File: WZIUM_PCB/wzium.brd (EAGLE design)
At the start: 100 x 100 mm, 21 parts, among them IC1 ATMEGA328PB-AU, J2 RASPBERRYPI-40-PIN-GPIO_PTH_M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

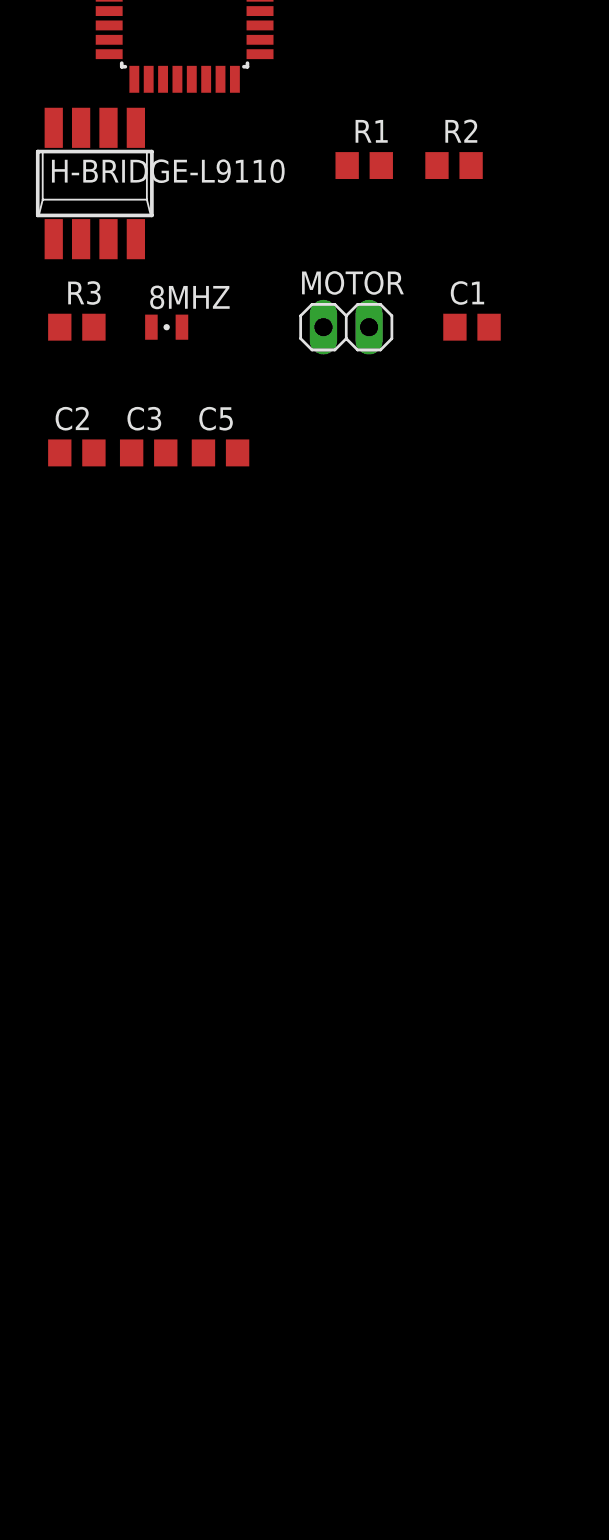
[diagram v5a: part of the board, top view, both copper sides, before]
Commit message: dodano sekcje czujnikow odleglosci Sharp GP2Y0A41SK0F
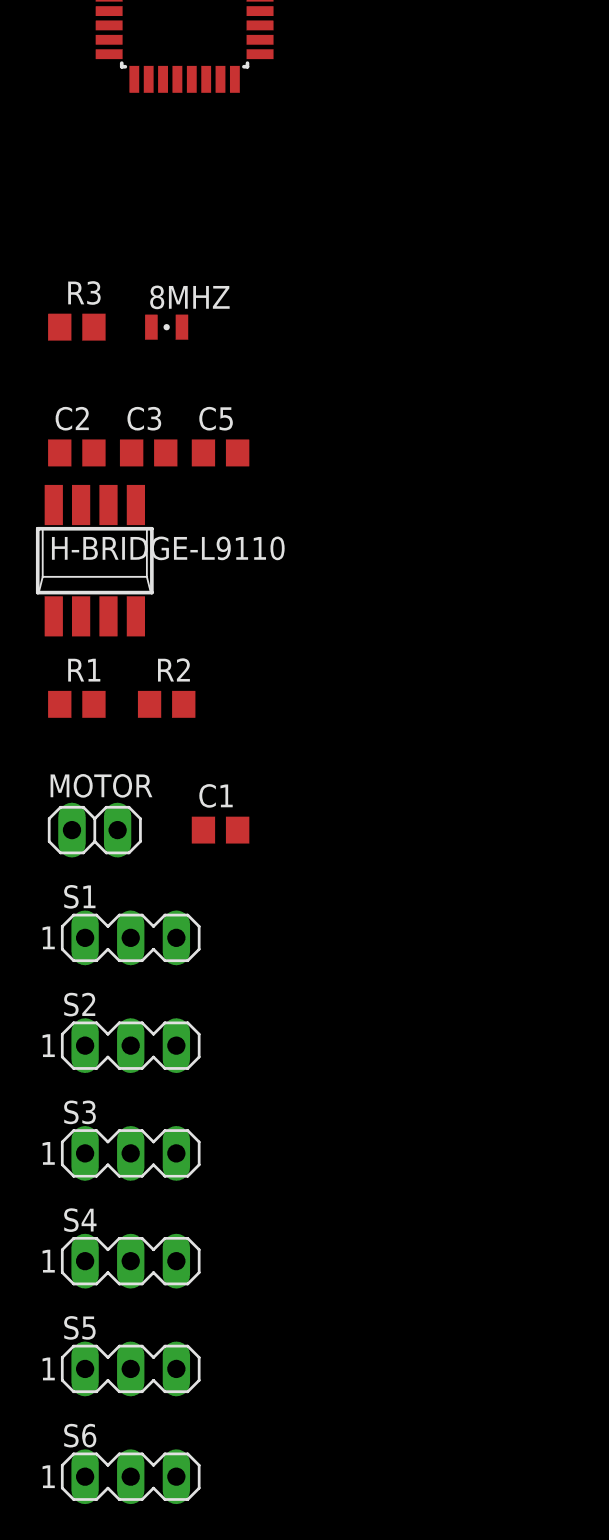
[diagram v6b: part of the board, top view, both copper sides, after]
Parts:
- added S1, S2, S3, S4, S5, S6: (no value), con-lstb:MA03-1
- moved R1 34.0 mm to (-6.00, -58.0)
- moved R2 34.0 mm to (-1.00, -58.0)
- moved C1 31.3 mm to (2.00, -65.0)
- moved MOTOR 31.3 mm to (-5.00, -65.0)
- moved H-BRIDGE-L9110 21.0 mm to (-5.00, -50.0)
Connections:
- new net S1OUT: IC1.23, S1.1
- new net S2OUT: IC1.24, S2.1
- new net S3OUT: IC1.25, S3.1
- new net S4OUT: IC1.26, S4.1
- new net S5OUT: IC1.27, S5.1
- new net S6OUT: IC1.28, S6.1
- net GND: now also S1.2, S2.2, S3.2, S4.2, S5.2, S6.2
- net VCC: now also S1.3, S2.3, S3.3, S4.3, S5.3, S6.3
